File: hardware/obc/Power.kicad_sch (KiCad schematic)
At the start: 42 parts, among them Q104 PMBT2222A, Q108 IRF9393, U401 TPS7A4501DCQT, U403 TPS54226PWPRPWP14_2P31X2P46-L, U404 ADM1176-1ARMZ-R7, U405 BQ25886RGER

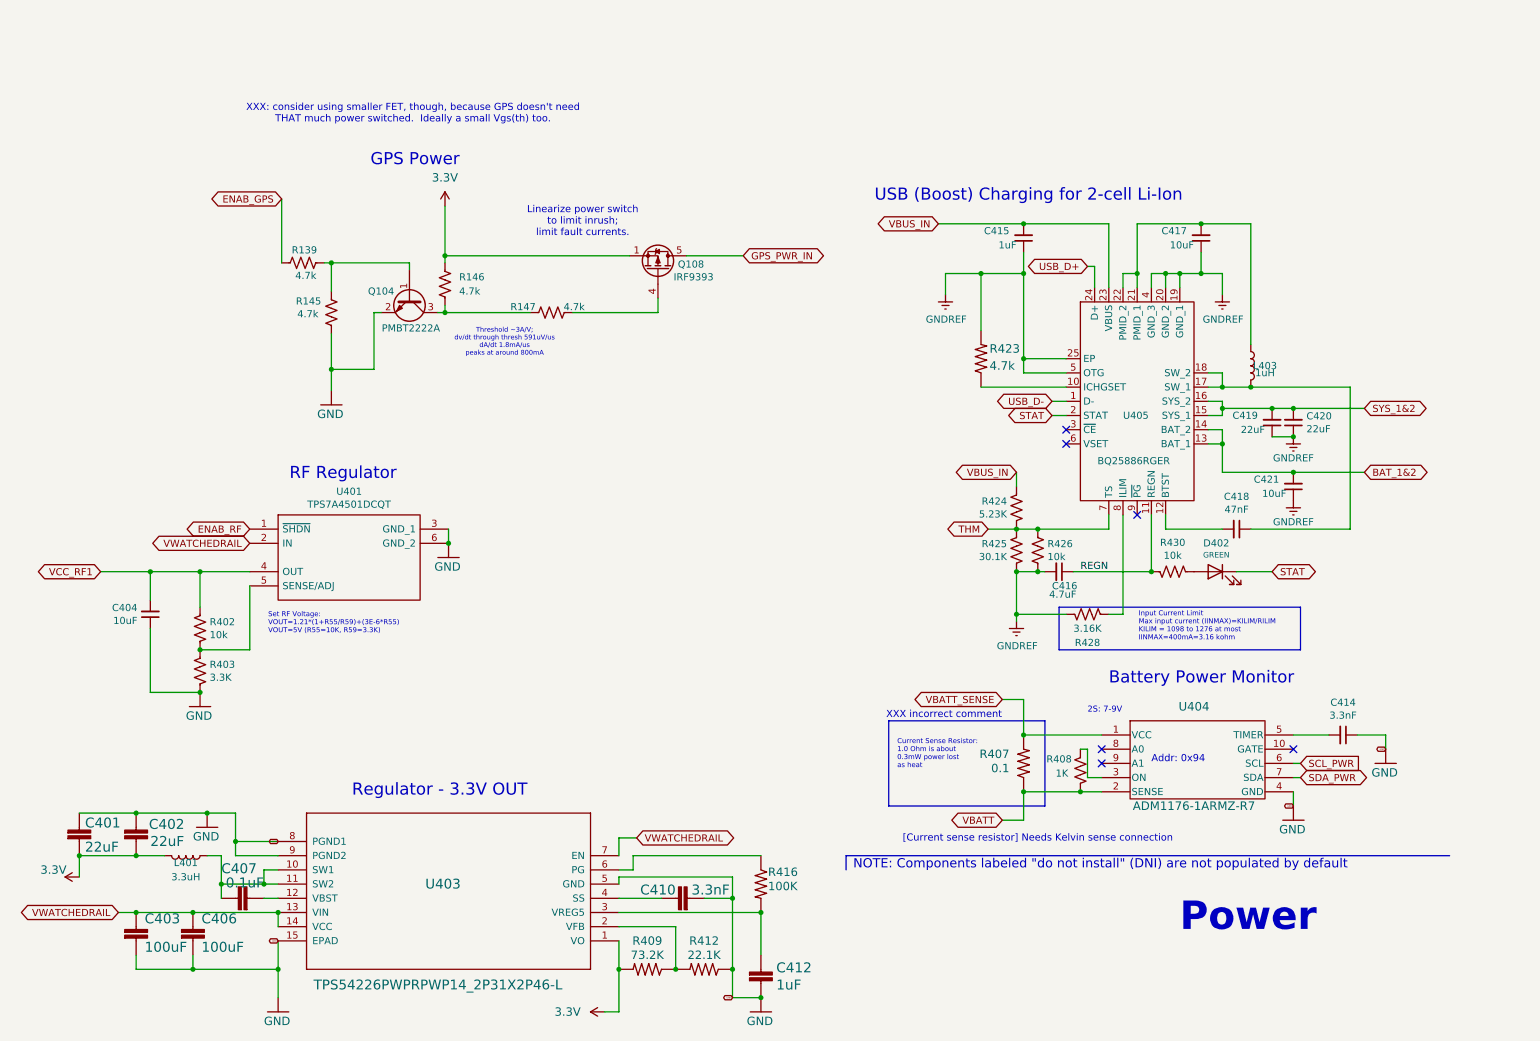
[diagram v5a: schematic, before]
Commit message: obc: Fixed second design review, and fixed up BOM
- added layout comments on schematic
- fixed various comments
- added many LCSC # for components
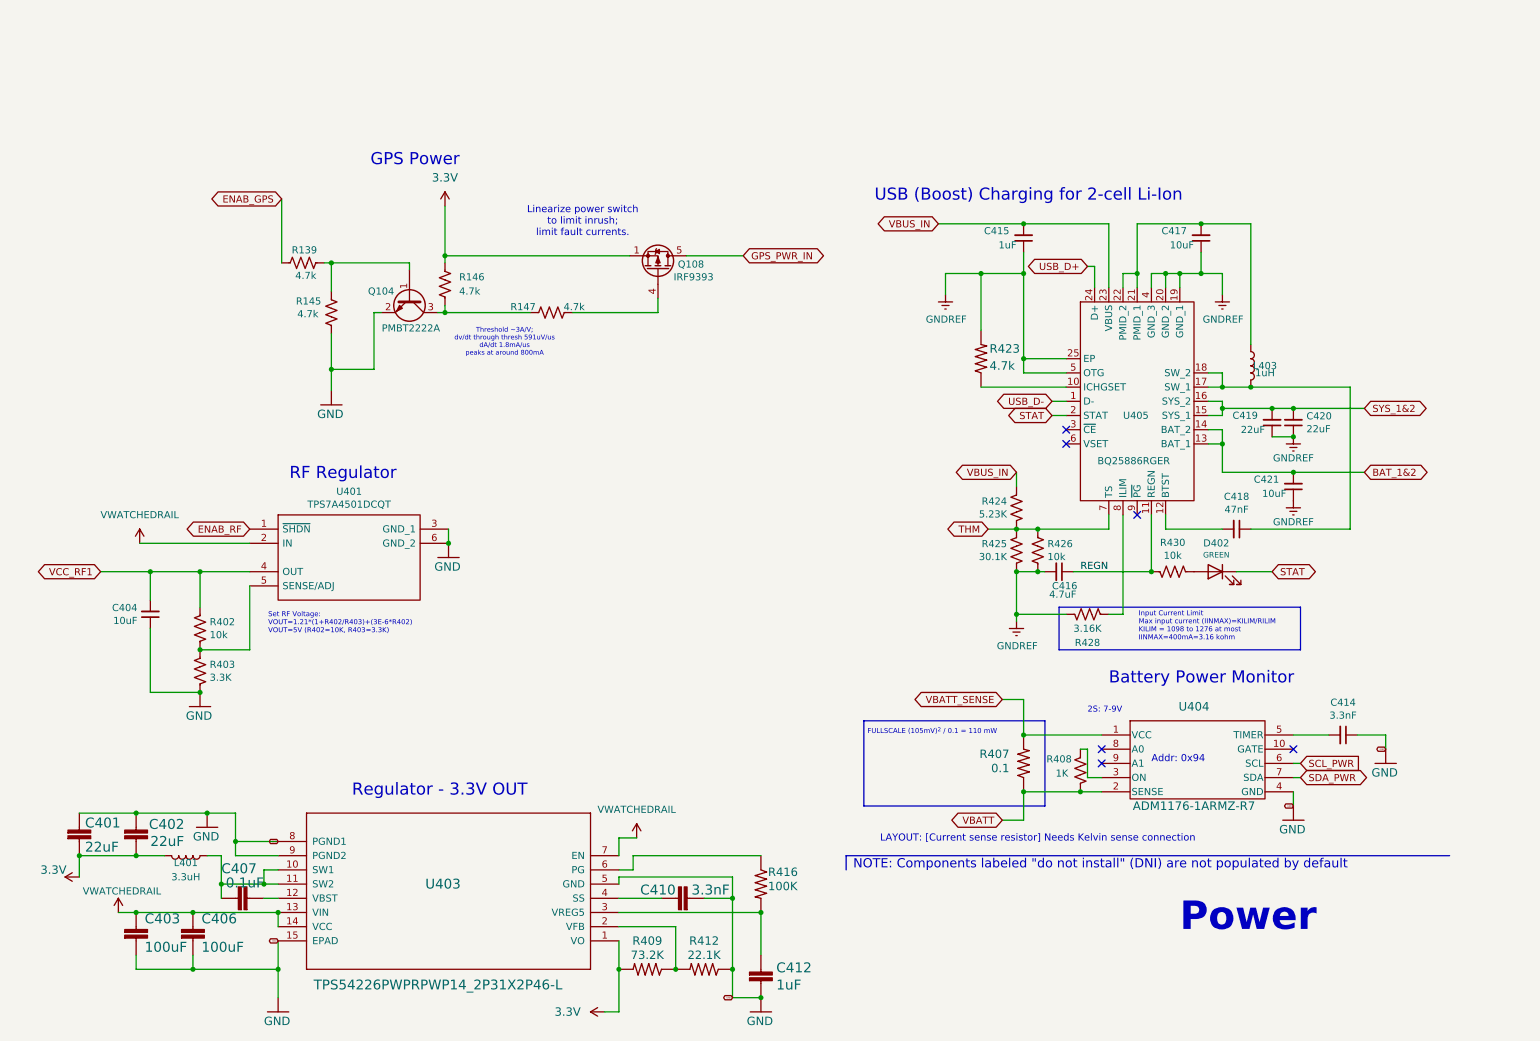
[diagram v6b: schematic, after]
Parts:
- R139, R145, R146, R147: LCSC (none) -> C23162
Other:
- note added: "FULLSCALE (105mV)^{2} / 0.1 = 110 mW"
- note added: "LAYOUT: [Current sense resistor] Needs Kelvin sense connection"
- note added: "Set RF Voltage: VOUT=1.21*(1+R402/R403)+(3E-6*R402) VOUT=5V (R402=10K, R403=3.3K)"
- note removed: "Current Sense Resistor: 1.0 Ohm is about 0.3mW power lost as heat"
- note removed: "Set RF Voltage: VOUT=1.21*(1+R55/R59)+(3E-6*R55) VOUT=5V (R55=10K, R59=3.3K)"
- note removed: "XXX incorrect comment"
- note removed: "XXX: consider using smaller FET, though, because GPS doesn't need THAT much power switched. Ideally a small Vgs(th) too."
- note removed: "[Current sense resistor] Needs Kelvin sense connection"

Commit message: obc: PCB work done towards next revision
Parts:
- R408: value 1K -> 1k
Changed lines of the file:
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@@
 			)
 		)
-		(property "Value" "1K"
+		(property "Value" "1k"
 			(at 198.628 154.178 0)
 			(effects

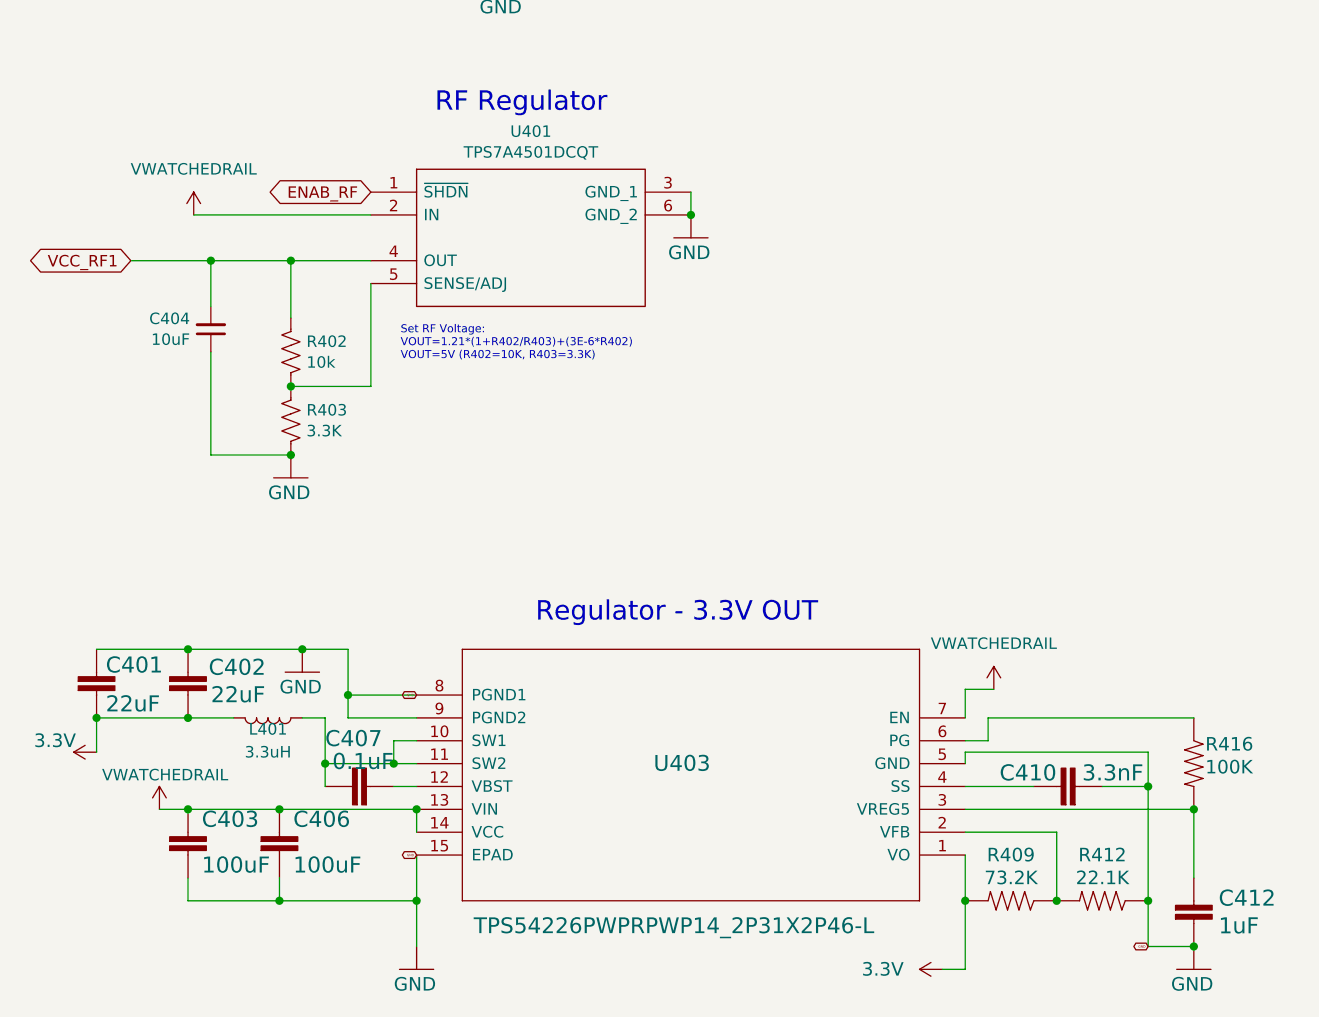
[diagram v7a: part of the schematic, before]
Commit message: obc: final cleanup before review
ex. cleaned wires in PCB, made text nicer on the schematic
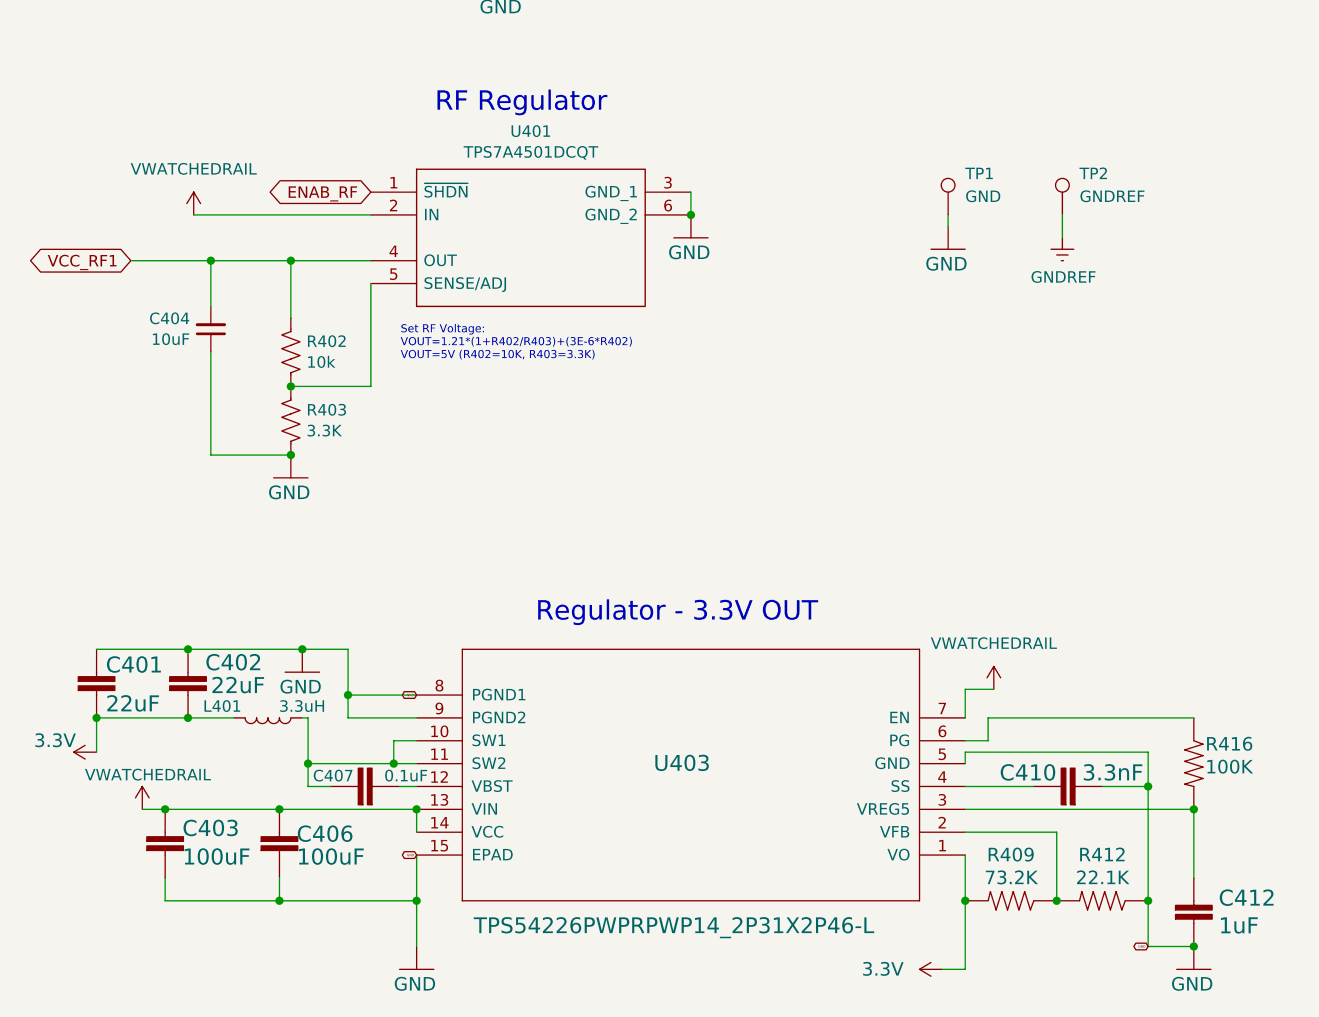
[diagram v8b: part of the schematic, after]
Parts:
- added TP1: GND, TestPoint:TestPoint_Keystone_5010-5014_Multipurpose, symbol Connector:TestPoint
- added TP2: GNDREF, TestPoint:TestPoint_Keystone_5010-5014_Multipurpose, symbol Connector:TestPoint
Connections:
- net GND: now also TP1.1
- net GNDREF: now also TP2.1
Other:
- moved on the sheet: C403, C407
